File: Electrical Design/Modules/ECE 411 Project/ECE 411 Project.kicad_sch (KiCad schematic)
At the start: 42 parts, among them J1 5mm 9V Barrel, J2 BOOST, J3 Pheonix Connector, J4 1/8in Jack, J5 1/4in Jack, SW1 SW_Push, SW2 SW_Push, SW3 SW_Push, SW4 SW_Push, SW5 SW_Push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

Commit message: pcb amp revision
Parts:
- removed CLK1: TestPoint, TestPoint:TestPoint_THTPad_2.5x2.5mm_Drill1.2mm, symbol Connector:TestPoint
- removed J5: 1/4in Jack, Connector_PinSocket_2.54mm:PinSocket_1x02_P2.54mm_Vertical, symbol Connector_Audio:AudioJack2
- added J5: 01x02 pin header, Connector_PinSocket_2.54mm:PinSocket_1x02_P2.54mm_Vertical, symbol Connector:Conn_01x02_Pin
- RV1, RV2, RV3, RV7: footprint Connector_PinSocket_2.54mm:PinSocket_1x03_P2.54mm_Vertical -> Connector_PinSocket_2.54mm:PinSocket_1x02_P2.54mm_Vertical
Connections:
- net GND: now also J5.1 (Pin_1)
- net LineOut: now also J5.2 (Pin_2)
- no-connect marks 7 -> 8
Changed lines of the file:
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@@
 	)
 	(junction
-		(at 135.255 52.07)
-		(diameter 0)
-		(color 0 0 0 0)
-	)
-	(junction
 		(at 36.195 158.75)
 		(diameter 0)
@@
 	)
 	(no_connect
+		(at 166.37 75.565)
+	)
+	(no_connect
 		(at 116.84 93.345)
 	)
@@
 	(wire
 		(pts
-			(xy 116.84 52.07) (xy 116.84 75.565)
-		)
-		(stroke
-			(width 0)
-			(type default)
-		)
-	)
-	(wire
-		(pts
 			(xy 50.165 158.75) (xy 36.195 158.75)
 		)
@@
 	(wire
 		(pts
-			(xy 155.575 75.565) (xy 155.575 52.07)
-		)
-		(stroke
-			(width 0)
-			(type default)
-		)
-	)
-	(wire
-		(pts
 			(xy 66.675 98.425) (xy 76.835 98.425)
 		)
@@
 	(wire
 		(pts
-			(xy 135.255 52.07) (xy 116.84 52.07)
-		)
-		(stroke
-			(width 0)
-			(type default)
-		)
-	)
-	(wire
-		(pts
 			(xy 38.735 26.035) (xy 45.085 26.035)
 		)
@@
 	(wire
 		(pts
-			(xy 159.385 62.23) (xy 166.37 62.23)
-		)
-		(stroke
-			(width 0)
-			(type default)
-		)
-	)
-	(wire
-		(pts
 			(xy 113.03 78.74) (xy 117.475 78.74)
 		)
@@
 	(wire
 		(pts
-			(xy 116.84 75.565) (xy 125.73 75.565)
-		)
-		(stroke
-			(width 0)
-			(type default)
-		)
-	)
-	(wire
-		(pts
 			(xy 94.615 179.705) (xy 94.615 184.15)
 		)
@@
 	(wire
 		(pts
-			(xy 155.575 52.07) (xy 135.255 52.07)
-		)
-		(stroke
-			(width 0)
-			(type default)
-		)
-	)
-	(wire
-		(pts
 			(xy 106.045 23.495) (xy 106.045 26.67)
 		)
@@
 	(wire
 		(pts
-			(xy 159.385 59.055) (xy 159.385 62.23)
-		)
-		(stroke
-			(width 0)
-			(type default)
-		)
-	)
-	(wire
-		(pts
 			(xy 104.775 184.15) (xy 104.775 168.91)
 		)
@@
 	(wire
 		(pts
+			(xy 163.83 62.23) (xy 166.37 62.23)
+		)
+		(stroke
+			(width 0)
+			(type default)
+		)
+	)
+	(wire
+		(pts
 			(xy 221.615 79.375) (xy 221.615 86.995)
 		)
@@
 	(wire
 		(pts
-			(xy 41.91 67.31) (xy 41.91 43.815)
+			(xy 163.83 58.42) (xy 163.83 62.23)
 		)
 		(stroke
@@
 	(wire
 		(pts
-			(xy 221.615 95.25) (xy 223.52 95.25)
+			(xy 41.91 67.31) (xy 41.91 43.815)
 		)
 		(stroke
@@
 	(wire
 		(pts
-			(xy 220.98 64.77) (xy 226.06 64.77)
+			(xy 221.615 95.25) (xy 223.52 95.25)
 		)
 		(stroke
@@
 	(wire
 		(pts
-			(xy 15.875 35.56) (xy 15.875 29.21)
+			(xy 220.98 64.77) (xy 226.06 64.77)
 		)
 		(stroke
@@
 	(wire
 		(pts
-			(xy 67.31 120.015) (xy 71.755 120.015)
+			(xy 15.875 35.56) (xy 15.875 29.21)
 		)
 		(stroke
@@
 	(wire
 		(pts
-			(xy 15.875 71.755) (xy 15.875 67.31)
+			(xy 67.31 120.015) (xy 71.755 120.015)
 		)
 		(stroke
@@
 	(wire
 		(pts
-			(xy 46.99 121.285) (xy 46.99 120.015)
+			(xy 15.875 71.755) (xy 15.875 67.31)
 		)
 		(stroke
@@
 	(wire
 		(pts
-			(xy 38.735 29.21) (xy 38.735 28.575)
+			(xy 46.99 121.285) (xy 46.99 120.015)
 		)
 		(stroke
@@
 	(wire
 		(pts
-			(xy 166.37 75.565) (xy 155.575 75.565)
+			(xy 38.735 29.21) (xy 38.735 28.575)
 		)
 		(stroke
@@
 	)
 	(rectangle
-		(start 254.635 30.48)
-		(end 283.21 46.99)
+		(start 248.285 30.48)
+		(end 281.305 46.99)
 		(stroke
 			(width 0)
@@
 	(global_label "+9V"
 		(shape output)
-		(at 159.385 59.055 90)
+		(at 163.83 58.42 90)
 		(fields_autoplaced yes)
 		(effects
@@
 		)
 		(property "Intersheetrefs" "${INTERSHEET_REFS}"
-			(at 159.385 52.1993 90)
+			(at 163.83 51.5643 90)
 			(effects
 				(font
@@
 			)
 		)
-		(property "Footprint" "Connector_PinSocket_2.54mm:PinSocket_1x03_P2.54mm_Vertical"
+		(property "Footprint" "Connector_PinSocket_2.54mm:PinSocket_1x02_P2.54mm_Vertical"
 			(at 210.185 79.375 0)
 			(effects
@@
 		(dnp no)
 		(property "Reference" "RV3"
-			(at 189.865 96.52 90)
+			(at 194.31 96.52 90)
 			(effects
 				(font
@@
 		)
 		(property "Value" "10k"
-			(at 189.865 99.06 90)
+			(at 194.31 99.06 90)
 			(effects
 				(font
@@
 			)
 		)
-		(property "Footprint" "Connector_PinSocket_2.54mm:PinSocket_1x03_P2.54mm_Vertical"
+		(property "Footprint" "Connector_PinSocket_2.54mm:PinSocket_1x02_P2.54mm_Vertical"
 			(at 194.31 93.345 0)
 			(effects
@@
 		(on_board yes)
 		(dnp no)
-		(fields_autoplaced yes)
 		(property "Reference" "RV2"
 			(at 154.305 96.52 90)
@@
 			)
 		)
-		(property "Footprint" "Connector_PinSocket_2.54mm:PinSocket_1x03_P2.54mm_Vertical"
+		(property "Footprint" "Connector_PinSocket_2.54mm:PinSocket_1x02_P2.54mm_Vertical"
 			(at 154.305 93.345 0)
 			(effects
@@
 	(symbol
 		(lib_id "Connector:TestPoint")
-		(at 135.255 52.07 0)
-		(unit 1)
-		(exclude_from_sim no)
-		(in_bom yes)
-		(on_board yes)
-		(dnp no)
-		(fields_autoplaced yes)
-		(property "Reference" "CLK1"
-			(at 137.16 47.4979 0)
-			(effects
-				(font
-					(size 1.27 1.27)
-				)
-				(justify left)
-			)
-		)
-		(property "Value" "TestPoint"
-			(at 137.16 50.0379 0)
-			(effects
-				(font
-					(size 1.27 1.27)
-				)
-				(justify left)
-			)
-		)
-		(property "Footprint" "TestPoint:TestPoint_THTPad_2.5x2.5mm_Drill1.2mm"
-			(at 140.335 52.07 0)
-			(effects
-				(font
-					(size 1.27 1.27)
-				)
-				(hide yes)
-			)
-		)
-		(property "Datasheet" "~"
-			(at 140.335 52.07 0)
-			(effects
-				(font
-					(size 1.27 1.27)
-				)
-				(hide yes)
-			)
-		)
-		(property "Description" "test point"
-			(at 135.255 52.07 0)
-			(effects
-				(font
-					(size 1.27 1.27)
-				)
-				(hide yes)
-			)
-		)
-		(pin "1"
-		)
-		(instances
-			(project "ECE 411 Project"
-				(path "/2625e5a1-d0c8-41ce-941d-75d035a5f1c5"
-					(reference "CLK1")
-					(unit 1)
-				)
-			)
-		)
-	)
-	(symbol
-		(lib_id "Connector:TestPoint")
 		(at 158.75 78.74 180)
 		(unit 1)
@@
 			)
 		)
-		(property "Footprint" "Connector_PinSocket_2.54mm:PinSocket_1x03_P2.54mm_Vertical"
+		(property "Footprint" "Connector_PinSocket_2.54mm:PinSocket_1x02_P2.54mm_Vertical"
 			(at 113.03 93.345 0)
 			(effects
@@
 	)
 	(symbol
-		(lib_id "Connector_Audio:AudioJack2")
-		(at 266.065 34.925 180)
-		(unit 1)
-		(exclude_from_sim no)
-		(in_bom yes)
-		(on_board yes)
-		(dnp no)
-		(property "Reference" "J5"
-			(at 263.525 40.64 0)
-			(effects
-				(font
-					(size 1.27 1.27)
-				)
-				(justify right)
-			)
-		)
-		(property "Value" "1/4in Jack"
-			(at 263.525 43.18 0)
-			(effects
-				(font
-					(size 1.27 1.27)
-				)
-				(justify right)
-			)
-		)
-		(property "Footprint" "Connector_PinSocket_2.54mm:PinSocket_1x02_P2.54mm_Vertical"
-			(at 266.065 34.925 0)
-			(effects
-				(font
-					(size 1.27 1.27)
-				)
-				(hide yes)
-			)
-		)
-		(property "Datasheet" "~"
-			(at 266.065 34.925 0)
-			(effects
-				(font
-					(size 1.27 1.27)
-				)
-				(hide yes)
-			)
-		)
-		(property "Description" "Audio Jack, 2 Poles (Mono / TS)"
-			(at 266.065 34.925 0)
-			(effects
-				(font
-					(size 1.27 1.27)
-				)
-				(hide yes)
-			)
-		)
-		(pin "S"
-		)
-		(pin "T"
-		)
-		(instances
-			(project ""
-				(path "/2625e5a1-d0c8-41ce-941d-75d035a5f1c5"
-					(reference "J5")
-					(unit 1)
-				)
-			)
-		)
-	)
-	(symbol
 		(lib_id "Regulator_Linear:HT75xx-1-SOT89")
 		(at 59.69 122.555 0)
@@
 					(unit 1)
 				)
+			)
+		)
+	)
+	(symbol
+		(lib_id "Connector:Conn_01x02_Pin")
+		(at 266.065 37.465 180)
+		(unit 1)
+		(exclude_from_sim no)
+		(in_bom yes)
+		(on_board yes)
+		(dnp no)
+		(property "Reference" "J5"
+			(at 262.255 39.37 0)
+			(effects
+				(font
+					(size 1.27 1.27)
+				)
+				(justify right)
+			)
+		)
+		(property "Value" "01x02 pin header"
+			(at 262.255 41.275 0)
+			(effects
+				(font
+					(size 1.27 1.27)
+				)
+				(justify right)
+			)
+		)
+		(property "Footprint" "Connector_PinSocket_2.54mm:PinSocket_1x02_P2.54mm_Vertical"
+			(at 266.065 37.465 0)
+			(effects
+				(font
+					(size 1.27 1.27)
+				)
+				(hide yes)
+			)
+		)
+		(property "Datasheet" "~"
+			(at 266.065 37.465 0)
+			(effects
+				(font
+					(size 1.27 1.27)
+				)
+				(hide yes)
+			)
+		)
+		(property "Description" "Generic connector, single row, 01x02, script generated"
+			(at 266.065 37.465 0)
+			(effects
+				(font
+					(size 1.27 1.27)
+				)
+				(hide yes)
+			)
+		)
+		(pin "1"
+		)
+		(pin "2"
+		)
+		(instances
+			(project ""
+				(path "/2625e5a1-d0c8-41ce-941d-75d035a5f1c5"
+					(reference "J5")
+					(unit 1)
+				)

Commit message: pcb redo b2.1
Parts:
- removed SW8: SW_Push, Connector_PinHeader_2.54mm:PinHeader_1x02_P2.54mm_Vertical, symbol Switch:SW_Push
- added J6, J7: 1x2header, Connector_PinSocket_2.54mm:PinSocket_1x02_P2.54mm_Vertical, symbol Connector:Conn_01x02_Pin
- added R9: 4.7k, Resistor_SMD:R_0805_2012Metric_Pad1.20x1.40mm_HandSolder, symbol Device:R
- added RV8: 100k, Connector_PinSocket_2.54mm:PinSocket_1x03_P2.54mm_Vertical, symbol Device:R_Potentiometer
- added SW10: SW_SPDT, Button_Switch_THT:SW_Slide_SPDT_Angled_CK_OS102011MA1Q, symbol Switch:SW_SPDT
- added TP1: Line In, TestPoint:TestPoint_Bridge_Pitch2.0mm_Drill0.7mm, symbol Connector:TestPoint
- J5: value 01x02 pin header -> 1x2 header
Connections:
- net ESP32-S3-WROOM Dev Board/BTN2 is gone; now on net ESP32-S3-WROOM Dev Board/BTN1: SW3.2
- net +4.5V: now also J6.2 (Pin_2)
- net +9V: now also J7.2 (Pin_2)
- net Chorus Effect/CHORUSIN: now also SW10.1 (A); no longer FUZ-CHO1.1, RV1.2, RV2.1
- net GND: now also RV8.3
- net LineIn: now also TP1.1
- net ESP32-S3-WROOM Dev Board/GENOUT renamed FX
- net ESP32-S3-WROOM Dev Board/SCL renamed SCL
- net ESP32-S3-WROOM Dev Board/SDA renamed SDA
- net Tremolo Effect/TREMOUT renamed Amp
- new net: RV2.1, SW10.3 (C)
- new net: R9.1, RV8.2
- new net Chorus Effect/V.5in: J6.1 (Pin_1)
- new net Chorus Effect/Vin: J7.1 (Pin_1)
- new net ESP32-S3-WROOM Dev Board/FREQ: RV8.1
- new net ESP32-S3-WROOM Dev Board/MCU3v3: R9.2
- new net Fuzz Schematic/FUZZOUT: FUZ-CHO1.1, RV1.2, SW10.2 (B)
- no-connect marks 8 -> 9
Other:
- sheet ESP32-S3-WROOM Dev Board ports: added FREQ, MCU3v3; removed BTN7
- note added: "Chorus Bypass"
- note added: "Chorus Clock Ctrl"
- note added: "Fuzz Ctrl"
- note added: "Tremolo Adj"
- moved on the sheet: FUZ-CHO1, J4, SW1, SW2, SW3, SW4, SW5, SW6, SW7

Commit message: new space-optimized PCB layout
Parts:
- added D4: LED, LED_THT:LED_D5.0mm, symbol Device:LED
- added R11: 1.2k, Resistor_SMD:R_0805_2012Metric_Pad1.20x1.40mm_HandSolder, symbol Device:R
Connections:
- net +5V: now also R11.1
- net GND: now also D4.1 (K)
- new net: D4.2 (A), R11.2
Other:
- note added: "Analog Music Synthesizer Modules"
- note added: "Chorus Disable"
- note added: "NOTES: - CHORUS MODULE CAN BE UNSTABLE: BYPASS USING SW10 TO DIVERT SIGNAL TO TREMOLO AND REMOVE JUMPERS J6/J7 TO CUT POWER TO CHORUS MODULE. - AUDIO AMPLIFIER OUTPUT POWER IS LIMITED BY INPUT SUPPLY RATING. - I^{2}C OLED MODULE HAS PULL-UP RESISTORS BUILT-IN - AUX INPUT FOR USING BOARD IN AMP-ONLY MODE OR FOR CONNECTING EXTERNAL SYNTH, GENERATOR, OR OTHER SIGNAL TO FX - J5 HEADER BREAKS OUT TO 1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"
- note removed: "Analog Music Synthesizer System"
- moved on the sheet: J6, J7

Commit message: add testpoints
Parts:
- CHO-TRE1, FUZ-CHO1, V4.5, V9, VGND1: footprint TestPoint:TestPoint_THTPad_2.5x2.5mm_Drill1.2mm -> TestPoint:TestPoint_Loop_D3.80mm_Drill2.5mm
- LINE_{IN}1: renamed from TP1; footprint TestPoint:TestPoint_Bridge_Pitch2.0mm_Drill0.7mm -> TestPoint:TestPoint_Loop_D3.80mm_Drill2.5mm
- LINE_{OUT}1: renamed from OUT_{LINE}1; footprint TestPoint:TestPoint_THTPad_2.5x2.5mm_Drill1.2mm -> TestPoint:TestPoint_Loop_D3.80mm_Drill2.5mm
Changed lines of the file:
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@@
 			)
 		)
-		(property "Footprint" "TestPoint:TestPoint_THTPad_2.5x2.5mm_Drill1.2mm"
+		(property "Footprint" "TestPoint:TestPoint_Loop_D3.80mm_Drill2.5mm"
 			(at 83.82 137.16 0)
 			(effects
@@
 		(on_board yes)
 		(dnp no)
-		(property "Reference" "OUT_{LINE}1"
+		(property "Reference" "LINE_{OUT}1"
 			(at 210.185 73.66 0)
 			(effects
@@
 			)
 		)
-		(property "Footprint" "TestPoint:TestPoint_THTPad_2.5x2.5mm_Drill1.2mm"
+		(property "Footprint" "TestPoint:TestPoint_Loop_D3.80mm_Drill2.5mm"
 			(at 209.55 79.375 0)
 			(effects
@@
 			(project "ECE 411 Project"
 				(path "/2625e5a1-d0c8-41ce-941d-75d035a5f1c5"
-					(reference "OUT_{LINE}1")
+					(reference "LINE_{OUT}1")
 					(unit 1)
 				)
@@
 			)
 		)
-		(property "Footprint" "TestPoint:TestPoint_THTPad_2.5x2.5mm_Drill1.2mm"
+		(property "Footprint" "TestPoint:TestPoint_Loop_D3.80mm_Drill2.5mm"
 			(at 153.67 78.74 0)
 			(effects
@@
 			)
 		)
-		(property "Footprint" "TestPoint:TestPoint_THTPad_2.5x2.5mm_Drill1.2mm"
+		(property "Footprint" "TestPoint:TestPoint_Loop_D3.80mm_Drill2.5mm"
 			(at 127.635 136.525 0)
 			(effects
@@
 			)
 		)
-		(property "Footprint" "TestPoint:TestPoint_THTPad_2.5x2.5mm_Drill1.2mm"
+		(property "Footprint" "TestPoint:TestPoint_Loop_D3.80mm_Drill2.5mm"
 			(at 73.66 158.75 0)
 			(effects
@@
 			)
 		)
-		(property "Footprint" "TestPoint:TestPoint_THTPad_2.5x2.5mm_Drill1.2mm"
+		(property "Footprint" "TestPoint:TestPoint_Loop_D3.80mm_Drill2.5mm"
 			(at 122.555 78.74 0)
 			(effects
@@
 		(dnp no)
 		(fields_autoplaced yes)
-		(property "Reference" "TP1"
+		(property "Reference" "LINE_{IN}1"
 			(at 44.45 96.3929 0)
 			(effects
@@
 			)
 		)
-		(property "Footprint" "TestPoint:TestPoint_Bridge_Pitch2.0mm_Drill0.7mm"
+		(property "Footprint" "TestPoint:TestPoint_Loop_D3.80mm_Drill2.5mm"
 			(at 47.625 100.965 0)
 			(effects
@@
 			(project ""
 				(path "/2625e5a1-d0c8-41ce-941d-75d035a5f1c5"
-					(reference "TP1")
+					(reference "LINE_{IN}1")
 					(unit 1)
 				)

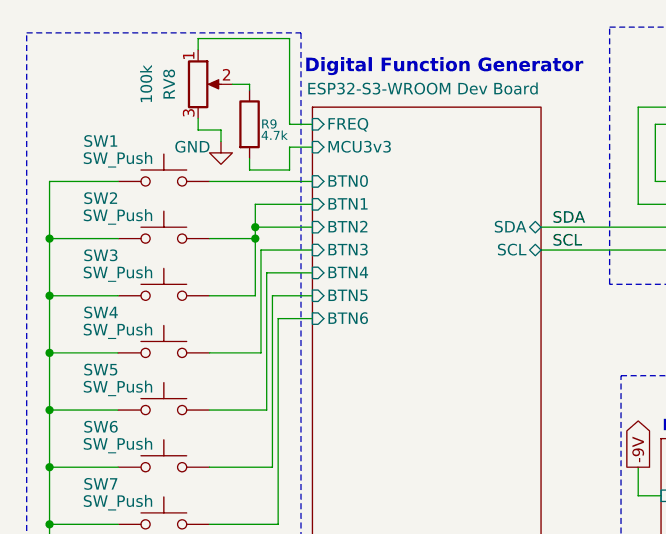
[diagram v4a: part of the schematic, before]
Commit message: update diode footptint, rounding edge cuts, some stitching
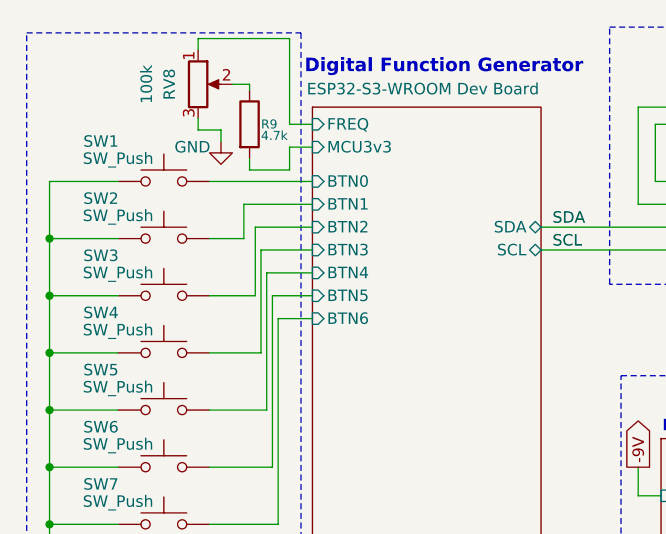
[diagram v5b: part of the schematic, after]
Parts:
- D2: footprint Diode_SMD:D_0805_2012Metric_Pad1.15x1.40mm_HandSolder -> Diode_THT:D_DO-41_SOD81_P10.16mm_Horizontal
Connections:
- net ESP32-S3-WROOM Dev Board/BTN1: no longer SW3.2
- new net ESP32-S3-WROOM Dev Board/BTN2: SW3.2
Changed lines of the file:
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@@
 		(title "SynthBuddy")
 		(date "2024-11-18")
-		(rev "r2.3")
+		(rev "r2.5")
 		(company "Portland State University")
 		(comment 1 "Open Source Hardware")
@@
 	)
 	(junction
-		(at 38.735 36.195)
-		(diameter 0)
-		(color 0 0 0 0)
-	)
-	(junction
 		(at 221.615 86.995)
 		(diameter 0)
@@
 	)
 	(junction
-		(at 38.735 34.925)
-		(diameter 0)
-		(color 0 0 0 0)
-	)
-	(junction
 		(at 132.715 136.525)
 		(diameter 0)
@@
 	(wire
 		(pts
-			(xy 38.735 42.545) (xy 38.735 36.195)
+			(xy 76.2 151.765) (xy 76.2 158.75)
 		)
 		(stroke
@@
 	(wire
 		(pts
-			(xy 76.2 151.765) (xy 76.2 158.75)
+			(xy 148.59 93.345) (xy 150.495 93.345)
 		)
 		(stroke
@@
 	(wire
 		(pts
-			(xy 148.59 93.345) (xy 150.495 93.345)
+			(xy 36.195 122.555) (xy 36.195 130.81)
 		)
 		(stroke
@@
 	(wire
 		(pts
-			(xy 36.195 122.555) (xy 36.195 130.81)
+			(xy 41.275 116.84) (xy 41.275 120.015)
 		)
 		(stroke
@@
 	(wire
 		(pts
-			(xy 41.275 116.84) (xy 41.275 120.015)
+			(xy 81.28 21.59) (xy 81.28 32.385)
 		)
 		(stroke
@@
 	(wire
 		(pts
-			(xy 81.28 21.59) (xy 81.28 32.385)
+			(xy 38.735 34.925) (xy 45.085 34.925)
 		)
 		(stroke
@@
 	(wire
 		(pts
-			(xy 38.735 32.385) (xy 45.085 32.385)
+			(xy 37.465 32.385) (xy 45.085 32.385)
 		)
 		(stroke
@@
 	(wire
 		(pts
-			(xy 38.735 34.925) (xy 45.085 34.925)
-		)
-		(stroke
-			(width 0)
-			(type default)
-		)
-	)
-	(wire
-		(pts
 			(xy 38.1 27.305) (xy 38.1 28.575)
 		)
@@
 	(wire
 		(pts
+			(xy 38.735 42.545) (xy 38.735 34.925)
+		)
+		(stroke
+			(width 0)
+			(type default)
+		)
+	)
+	(wire
+		(pts
 			(xy 46.99 137.16) (xy 50.165 137.16)
 		)
@@
 	(wire
 		(pts
-			(xy 33.655 36.195) (xy 38.735 36.195)
+			(xy 33.655 36.195) (xy 37.465 36.195)
 		)
 		(stroke
@@
 	(wire
 		(pts
-			(xy 38.735 36.195) (xy 38.735 34.925)
+			(xy 37.465 32.385) (xy 37.465 36.195)
 		)
 		(stroke
@@
 	(wire
 		(pts
-			(xy 38.735 34.925) (xy 38.735 32.385)
-		)
-		(stroke
-			(width 0)
-			(type default)
-		)
-	)
-	(wire
-		(pts
 			(xy 81.915 93.345) (xy 81.915 78.74)
 		)
@@
 			)
 		)
-		(property "Footprint" "Diode_SMD:D_0805_2012Metric_Pad1.15x1.40mm_HandSolder"
+		(property "Footprint" "Diode_THT:D_DO-41_SOD81_P10.16mm_Horizontal"
 			(at 50.165 147.955 0)
 			(effects

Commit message: pcb finalization
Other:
- note added: "NOTES: - CHORUS MODULE CAN BE UNSTABLE: BYPASS USING SW10 TO DIVERT SIGNAL TO TREMOLO AND REMOVE JUMPERS J6/J7 TO CUT POWER TO CHORUS MODULE - AUDIO AMPLIFIER OUTPUT POWER IS LIMITED BY INPUT SUPPLY RATING - I^{2}C OLED MODULE HAS PULL-UP RESISTORS BUILT-IN - AUX INPUT FOR USING BOARD IN AMP-ONLY MODE OR FOR CONNECTING EXTERNAL SYNTH, GENERATOR, OR OTHER SIGNAL TO FX - J5 HEADER BREAKS OUT TO 1/4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"
- note removed: "NOTES: - CHORUS MODULE CAN BE UNSTABLE: BYPASS USING SW10 TO DIVERT SIGNAL TO TREMOLO AND REMOVE JUMPERS J6/J7 TO CUT POWER TO CHORUS MODULE. - AUDIO AMPLIFIER OUTPUT POWER IS LIMITED BY INPUT SUPPLY RATING. - I^{2}C OLED MODULE HAS PULL-UP RESISTORS BUILT-IN - AUX INPUT FOR USING BOARD IN AMP-ONLY MODE OR FOR CONNECTING EXTERNAL SYNTH, GENERATOR, OR OTHER SIGNAL TO FX - J5 HEADER BREAKS OUT TO 1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"
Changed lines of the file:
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@@
 		)
 	)
-	(text "NOTES:\n- CHORUS MODULE CAN BE UNSTABLE: BYPASS USING SW10 TO DIVERT SIGNAL TO TREMOLO\nAND REMOVE JUMPERS J6/J7 TO CUT POWER TO CHORUS MODULE.\n- AUDIO AMPLIFIER OUTPUT POWER IS LIMITED BY INPUT SUPPLY RATING.\n- I^{2}C OLED MODULE HAS PULL-UP RESISTORS BUILT-IN\n- AUX INPUT FOR USING BOARD IN AMP-ONLY MODE OR FOR CONNECTING EXTERNAL\nSYNTH, GENERATOR, OR OTHER SIGNAL TO FX\n- J5 HEADER BREAKS OUT TO 1/4\" JACK"
+	(text "NOTES:\n- CHORUS MODULE CAN BE UNSTABLE: BYPASS USING SW10 TO DIVERT SIGNAL TO TREMOLO\nAND REMOVE JUMPERS J6/J7 TO CUT POWER TO CHORUS MODULE\n- AUDIO AMPLIFIER OUTPUT POWER IS LIMITED BY INPUT SUPPLY RATING\n- I^{2}C OLED MODULE HAS PULL-UP RESISTORS BUILT-IN\n- AUX INPUT FOR USING BOARD IN AMP-ONLY MODE OR FOR CONNECTING EXTERNAL\nSYNTH, GENERATOR, OR OTHER SIGNAL TO FX\n- J5 HEADER BREAKS OUT TO 1/4\" JACK"
 		(exclude_from_sim no)
 		(at 177.8 151.765 0)

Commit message: pcb madness
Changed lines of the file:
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@@
-	)
-	(junction
-		(at 203.2 79.375)
-		(diameter 0)
-		(color 0 0 0 0)
 	)
 	(junction
@@
 	(junction
 		(at 34.29 140.97)
+		(diameter 0)
+		(color 0 0 0 0)
+	)
+	(junction
+		(at 202.565 79.375)
 		(diameter 0)
 		(color 0 0 0 0)
@@
 	(wire
 		(pts
-			(xy 204.47 79.375) (xy 203.2 79.375)
-		)
-		(stroke
-			(width 0)
-			(type default)
-		)
-	)
-	(wire
-		(pts
 			(xy 99.06 110.49) (xy 106.045 110.49)
 		)
@@
 	(wire
 		(pts
-			(xy 194.31 79.375) (xy 203.2 79.375)
+			(xy 194.31 79.375) (xy 202.565 79.375)
 		)
 		(stroke
@@
 	(wire
 		(pts
-			(xy 71.755 106.045) (xy 203.2 106.045)
+			(xy 71.755 106.045) (xy 202.565 106.045)
 		)
 		(stroke
@@
 	(wire
 		(pts
-			(xy 203.2 106.045) (xy 203.2 79.375)
+			(xy 202.565 106.045) (xy 202.565 79.375)
 		)
 		(stroke
@@
 		)
 		(stroke
+			(width 0)
+			(type default)
+		)
+	)
+	(wire
+		(pts
+			(xy 202.565 79.375) (xy 204.47 79.375)
+		)
+		(stroke

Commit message: adding chorus test poiunts, touch ups
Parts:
- added GENOUT1: TestPoint, TestPoint:TestPoint_Loop_D3.80mm_Drill2.5mm, symbol Connector:TestPoint
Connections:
- net FX: now also GENOUT1.1
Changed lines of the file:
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@@
 	)
 	(junction
+		(at 72.39 78.74)
+		(diameter 0)
+		(color 0 0 0 0)
+	)
+	(junction
 		(at 62.865 137.16)
 		(diameter 0)
@@
 	(wire
 		(pts
-			(xy 70.485 78.74) (xy 76.835 78.74)
+			(xy 70.485 78.74) (xy 72.39 78.74)
 		)
 		(stroke
@@
 	(wire
 		(pts
+			(xy 72.39 78.74) (xy 76.835 78.74)
+		)
+		(stroke
+			(width 0)
+			(type default)
+		)
+	)
+	(wire
+		(pts
 			(xy 38.1 28.575) (xy 42.545 28.575)
 		)
@@
 					(unit 1)
 				)
+			)
+		)
+	)
+	(symbol
+		(lib_id "Connector:TestPoint")
+		(at 72.39 78.74 0)
+		(unit 1)
+		(exclude_from_sim no)
+		(in_bom yes)
+		(on_board yes)
+		(dnp no)
+		(property "Reference" "GENOUT1"
+			(at 71.755 70.485 0)
+			(effects
+				(font
+					(size 1 1)
+				)
+				(justify left)
+			)
+		)
+		(property "Value" "TestPoint"
+			(at 71.755 73.025 0)
+			(effects
+				(font
+					(size 1 1)
+				)
+				(justify left)
+			)
+		)
+		(property "Footprint" "TestPoint:TestPoint_Loop_D3.80mm_Drill2.5mm"
+			(at 77.47 78.74 0)
+			(effects
+				(font
+					(size 1.27 1.27)
+				)
+				(hide yes)
+			)
+		)
+		(property "Datasheet" "~"
+			(at 77.47 78.74 0)
+			(effects
+				(font
+					(size 1.27 1.27)
+				)
+				(hide yes)
+			)
+		)
+		(property "Description" "test point"
+			(at 72.39 78.74 0)
+			(effects
+				(font
+					(size 1.27 1.27)
+				)
+				(hide yes)
+			)
+		)
+		(pin "1"
+		)
+		(instances
+			(project ""
+				(path "/2625e5a1-d0c8-41ce-941d-75d035a5f1c5"
+					(reference "GENOUT1")
+					(unit 1)
+				)
